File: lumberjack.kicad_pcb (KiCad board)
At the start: 2 copper layers, 285.4 x 94.9 mm, 156 parts, among them J1 USB, J2 AVR_ISP_6, J3 JST, SW1 RESET, SW2 BOOT, U1 ATMEGA328-PU, Y1 16MHz

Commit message: Update lumberjack.kicad_pcb
Updated PCB file, removed all traces
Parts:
- removed C1, C2: 22p, Capacitor_THT:C_Disc_D3.0mm_W1.6mm_P2.50mm
- removed C3: 4.7u, Capacitor_THT:CP_Radial_D4.0mm_P1.50mm
- removed C4, C5: 100n, Capacitor_THT:C_Disc_D4.3mm_W1.9mm_P5.00mm
- removed D1, D10, D11, D12, D13, D14, D15, D16, D17, D18, D19, D2, D20, D21, D22, D23, D24, D25, D26, D27, D28, D29, D3, D30, D31, D32, D33, D34, D35, D36, D37, D38, D39, D4, D40, D41, D42, D43, D44, D45, D46, D47, D48, D49, D5, D50, D51, D52, D53, D54, D55, D56, D57, D58, D59, D6, D60, D7, D8, D9: 1N4148, Diode_THT:D_DO-35_SOD27_P7.62mm_Horizontal
- removed D61, D62: 3.6V, Diode_THT:D_DO-35_SOD27_P7.62mm_Horizontal
- removed F1: 100mA, Fuse:Fuse_Bourns_MF-RHT100
- removed J2: AVR_ISP_6, Connector_PinHeader_2.54mm:PinHeader_2x03_P2.54mm_Vertical
- removed J3: JST, Connector_JST:JST_SH_SM04B-SRSS-TB_1x04-1MP_P1.00mm_Horizontal
- removed LED2: GREEN, LED_THT:LED_D3.0mm
- removed REF**: flags, lumberjack:Flags
- removed REF**: OSHW-Logo_7.5x8mm_Copper, Symbol:OSHW-Logo_7.5x8mm_Copper
- removed SW1: RESET, Button_Switch_THT:SW_PUSH_6mm
- removed SW2: BOOT, Button_Switch_THT:SW_PUSH_6mm
- removed Y1: 16MHz, Crystal:Crystal_HC49-4H_Vertical
- added JBtn1: Conn_01x06_Male, Connector_PinSocket_2.54mm:PinSocket_1x06_P2.54mm_Vertical, F.Cu at (135.9, 17.8)
- added JBtn2: Conn_01x06_Male, Connector_PinSocket_2.54mm:PinSocket_1x06_P2.54mm_Vertical, F.Cu at (108.3, 17.8)
- added JConn1: Conn_01x06_Male, Connector_PinSocket_2.54mm:PinSocket_1x06_P2.54mm_Vertical, F.Cu at (66.0, 38.1)
- added JL1: Conn_01x06_Male, Connector_PinSocket_2.54mm:PinSocket_1x06_P2.54mm_Vertical, F.Cu at (108.3, 35.1)
- added JL2: Conn_01x06_Male, Connector_PinSocket_2.54mm:PinSocket_1x06_P2.54mm_Vertical, F.Cu at (122.1, 17.8)
- added JL3: Conn_01x06_Male, Connector_PinSocket_2.54mm:PinSocket_1x06_P2.54mm_Vertical, F.Cu at (112.9, 35.1)
- added JL4: Conn_01x06_Male, Connector_PinSocket_2.54mm:PinSocket_1x06_P2.54mm_Vertical, F.Cu at (126.7, 17.8)
- added JL5: Conn_01x06_Male, Connector_PinSocket_2.54mm:PinSocket_1x06_P2.54mm_Vertical, F.Cu at (117.5, 35.1)
- added JR1: Conn_01x06_Male, Connector_PinSocket_2.54mm:PinSocket_1x06_P2.54mm_Vertical, F.Cu at (131.3, 17.8)
- added JR2: Conn_01x06_Male, Connector_PinSocket_2.54mm:PinSocket_1x06_P2.54mm_Vertical, F.Cu at (112.9, 17.8)
- added JR3: Conn_01x06_Male, Connector_PinSocket_2.54mm:PinSocket_1x06_P2.54mm_Vertical, F.Cu at (140.5, 17.8)
- added JR4: Conn_01x06_Male, Connector_PinSocket_2.54mm:PinSocket_1x06_P2.54mm_Vertical, F.Cu at (122.1, 35.1)
- added JR5: Conn_01x06_Male, Connector_PinSocket_2.54mm:PinSocket_1x06_P2.54mm_Vertical, F.Cu at (157.5, 31.8)
- added R10: 47k, Resistor_THT:R_Axial_DIN0204_L3.6mm_D1.6mm_P7.62mm_Horizontal, F.Cu at (173.3, 19.2)
- added R11: 47k, Resistor_THT:R_Axial_DIN0204_L3.6mm_D1.6mm_P7.62mm_Horizontal, F.Cu at (173.3, 22.4)
- added R12: 47k, Resistor_THT:R_Axial_DIN0204_L3.6mm_D1.6mm_P7.62mm_Horizontal, F.Cu at (173.3, 25.5)
- added R13: 1.5k, Resistor_THT:R_Axial_DIN0204_L3.6mm_D1.6mm_P7.62mm_Horizontal, F.Cu at (144.2, 17.0)
- added R9: 47k, Resistor_THT:R_Axial_DIN0204_L3.6mm_D1.6mm_P7.62mm_Horizontal, F.Cu at (173.3, 16.1)
- added U2: 4021, Package_DIP:DIP-16_W7.62mm_LongPads, F.Cu at (96.3, 17.5)
- J1: value USB -> RJ45; footprint lumberjack:USB_Hybrid_THT -> Connector_RJ:RJ45_Amphenol_54602-x08_Horizontal
- R1, R7, R8: value 1.5k -> 47k
- R2, R3: value 75R -> 47k
- R4: value 10k -> 47k
- R5, R6: value 5.1k -> 47k
- U1: value ATMEGA328-PU -> 4021; footprint Package_DIP:DIP-28_W7.62mm -> Package_DIP:DIP-16_W7.62mm_LongPads
- moved R6 128.1 mm to (169.5, 32.3), turned to 180 degrees
- moved R5 126.5 mm to (169.5, 29.9), turned to 180 degrees
- moved U1 88.1 mm to (83.7, 17.0)
- moved R4 87.9 mm to (168.8, 18.9)
- moved R1 87.9 mm to (161.1, 26.1)
- moved R2 87.9 mm to (161.1, 23.7)
- moved R3 87.9 mm to (161.1, 21.3)
- moved J1 43.7 mm to (57.1, 30.5)
- moved R7 41.5 mm to (181.8, 31.7)
- moved R8 34.9 mm to (181.5, 29.1)
- moved LED1 20.6 mm to (146.1, 43.2)
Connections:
- 2u_MX30 pad 1: Net-(2u_MX30-Pad1) -> GND
- 2u_MX30 pad 2: /COL4 -> /L5.6
- 2u_MX60 pad 1: Net-(2u_MX60-Pad1) -> GND
- 2u_MX60 pad 2: /COL9 -> /R5.1
- MX1 pad 1: Net-(D1-Pad2) -> GND
- MX1 pad 2: /COL0 -> /L1.1
- MX10 pad 1: Net-(D10-Pad2) -> GND
- MX10 pad 2: /COL1 -> /L4.2
- MX11 pad 1: Net-(D11-Pad2) -> GND
- MX11 pad 2: /COL1 -> /L4.3
- MX12 pad 1: Net-(D12-Pad2) -> GND
- MX12 pad 2: /COL1 -> /L5.3
- MX13 pad 1: Net-(D13-Pad2) -> GND
- MX13 pad 2: /COL2 -> /L1.3
- MX14 pad 1: Net-(D14-Pad2) -> GND
- MX14 pad 2: /COL2 -> /L2.3
- MX15 pad 1: Net-(D15-Pad2) -> GND
- MX15 pad 2: /COL2 -> /L3.3
- MX16 pad 1: Net-(D16-Pad2) -> GND
- MX16 pad 2: /COL2 -> /L3.4
- MX17 pad 1: Net-(D17-Pad2) -> GND
- MX17 pad 2: /COL2 -> /L4.4
- MX18 pad 1: Net-(D18-Pad2) -> GND
- MX18 pad 2: /COL2 -> /L5.4
- MX19 pad 1: Net-(D19-Pad2) -> GND
- MX19 pad 2: /COL3 -> /L1.4
- MX2 pad 1: Net-(D2-Pad2) -> GND
- MX2 pad 2: /COL0 -> /L2.1
- MX20 pad 1: Net-(D20-Pad2) -> GND
- MX20 pad 2: /COL3 -> /L2.4
- MX21 pad 1: Net-(D21-Pad2) -> GND
- MX21 pad 2: /COL3 -> /L2.5
- MX22 pad 1: Net-(D22-Pad2) -> GND
- MX22 pad 2: /COL3 -> /L3.5
- MX23 pad 1: Net-(D23-Pad2) -> GND
- MX23 pad 2: /COL3 -> /L4.5
- MX24 pad 1: Net-(D24-Pad2) -> GND
- MX24 pad 2: /COL3 -> /L5.5
- MX25 pad 1: Net-(D25-Pad2) -> GND
- MX25 pad 2: /COL4 -> /L1.5
- MX26 pad 1: Net-(D26-Pad2) -> GND
- MX26 pad 2: /COL4 -> /L1.6
- MX27 pad 1: Net-(D27-Pad2) -> GND
- MX27 pad 2: /COL4 -> /L2.6
- MX28 pad 1: Net-(D28-Pad2) -> GND
- MX28 pad 2: /COL4 -> /L3.6
- MX29 pad 1: Net-(D29-Pad2) -> GND
- MX29 pad 2: /COL4 -> /L4.6
- MX3 pad 1: Net-(D3-Pad2) -> GND
- MX3 pad 2: /COL0 -> /L3.1
- MX30 pad 1: Net-(2u_MX30-Pad1) -> GND
- MX30 pad 2: /COL4 -> /L5.6
- MX31 pad 1: Net-(D31-Pad2) -> GND
- MX31 pad 2: /COL5 -> /R1.6
- MX32 pad 1: Net-(D32-Pad2) -> GND
- MX32 pad 2: /COL5 -> /R2.6
- MX33 pad 1: Net-(D33-Pad2) -> GND
- MX33 pad 2: /COL5 -> /R3.6
- MX34 pad 1: Net-(D34-Pad2) -> GND
- MX34 pad 2: /COL5 -> /R4.6
- MX35 pad 1: Net-(D35-Pad2) -> GND
- MX35 pad 2: /COL5 -> /R5.6
- MX36 pad 1: Net-(D36-Pad2) -> GND
- MX36 pad 2: /COL5 -> /R5.5
- MX37 pad 1: Net-(D37-Pad2) -> GND
- MX37 pad 2: /COL6 -> /R1.5
- MX38 pad 1: Net-(D38-Pad2) -> GND
- MX38 pad 2: /COL6 -> /R2.5
- MX39 pad 1: Net-(D39-Pad2) -> GND
- MX39 pad 2: /COL6 -> /R3.5
- MX4 pad 1: Net-(D4-Pad2) -> GND
- MX4 pad 2: /COL0 -> /L4.1
- MX40 pad 1: Net-(D40-Pad2) -> GND
- MX40 pad 2: /COL6 -> /R4.5
- MX41 pad 1: Net-(D41-Pad2) -> GND
- MX41 pad 2: /COL6 -> /R4.4
- MX42 pad 1: Net-(D42-Pad2) -> GND
- MX42 pad 2: /COL6 -> /R5.4
- MX43 pad 1: Net-(D43-Pad2) -> GND
- MX43 pad 2: /COL7 -> /R1.4
- MX44 pad 1: Net-(D44-Pad2) -> GND
- MX44 pad 2: /COL7 -> /R2.4
- MX45 pad 1: Net-(D45-Pad2) -> GND
- MX45 pad 2: /COL7 -> /R3.4
- MX46 pad 1: Net-(D46-Pad2) -> GND
- MX46 pad 2: /COL7 -> /R3.3
- MX47 pad 1: Net-(D47-Pad2) -> GND
- MX47 pad 2: /COL7 -> /R4.3
- MX48 pad 1: Net-(D48-Pad2) -> GND
- MX48 pad 2: /COL7 -> /R5.3
- MX49 pad 1: Net-(D49-Pad2) -> GND
- MX49 pad 2: /COL8 -> /R1.3
- MX5 pad 1: Net-(D5-Pad2) -> GND
- MX5 pad 2: /COL0 -> /L5.1
- MX50 pad 1: Net-(D50-Pad2) -> GND
- MX50 pad 2: /COL8 -> /R2.3
- MX51 pad 1: Net-(D51-Pad2) -> GND
- MX51 pad 2: /COL8 -> /R2.2
- MX52 pad 1: Net-(D52-Pad2) -> GND
- MX52 pad 2: /COL8 -> /R3.2
- MX53 pad 1: Net-(D53-Pad2) -> GND
- MX53 pad 2: /COL8 -> /R4.2
- MX54 pad 1: Net-(D54-Pad2) -> GND
- MX54 pad 2: /COL8 -> /R5.2
- MX55 pad 1: Net-(D55-Pad2) -> GND
- MX55 pad 2: /COL9 -> /R1.2
- MX56 pad 1: Net-(D56-Pad2) -> GND
- MX56 pad 2: /COL9 -> /R1.1
- MX57 pad 1: Net-(D57-Pad2) -> GND
- MX57 pad 2: /COL9 -> /R2.1
- MX58 pad 1: Net-(D58-Pad2) -> GND
- MX58 pad 2: /COL9 -> /R3.1
- MX59 pad 1: Net-(D59-Pad2) -> GND
- MX59 pad 2: /COL9 -> /R4.1
- MX6 pad 1: Net-(D6-Pad2) -> GND
- MX6 pad 2: /COL0 -> /L5.2
- MX60 pad 1: Net-(2u_MX60-Pad1) -> GND
- MX60 pad 2: /COL9 -> /R5.1
- MX7 pad 1: Net-(D7-Pad2) -> GND
- MX7 pad 2: /COL1 -> /L1.2
- MX8 pad 1: Net-(D8-Pad2) -> GND
- MX8 pad 2: /COL1 -> /L2.2
- MX9 pad 1: Net-(D9-Pad2) -> GND
- MX9 pad 2: /COL1 -> /L3.2
- R1 pad 1: Net-(D67-Pad1) -> /BtnUp
- R2 pad 1: Net-(D66-Pad1) -> /BtnDown
- R2 pad 2: /USB_D+ -> +5V
- R3 pad 1: Net-(D67-Pad1) -> /BtnLeft
- R3 pad 2: /USB_D- -> +5V
- R4 pad 1: +5V -> /BtnRight
- R4 pad 2: /RESET -> +5V
- R5 pad 1: GND -> /BtnStart
- R5 pad 2: Net-(J1-PadCC1) -> +5V
- R6 pad 1: GND -> /BtnSelect
- R6 pad 2: Net-(J1-PadCC2) -> +5V
- R7 pad 1: /LED1 -> /BtnA
- R7 pad 2: Net-(LED1-Pad2) -> +5V
- R8 pad 1: /LED2 -> /BtnB
- R8 pad 2: Net-(LED2-Pad2) -> +5V
- U1 pad 1: /RESET -> /BtnB
- U1 pad 10: Net-(C1-Pad1) -> /clock
- U1 pad 11: /COL3 -> Net-(U1-Pad11)
- U1 pad 12: /COL2 -> Net-(U1-Pad12)
- U1 pad 13: /COL1 -> /BtnStart
- U1 pad 14: /COL0 -> /BtnSelect
- U1 pad 15: /ROW5 -> /BtnY
- U1 pad 16: /ROW4 -> +5V
- U1 pad 2: /COL6 -> Net-(U1-Pad2)
- U1 pad 3: /COL5 -> /data
- U1 pad 4: /USB_D+ -> /BtnUp
- U1 pad 5: /USB_D- -> /BtnDown
- U1 pad 6: /COL4 -> /BtnLeft
- U1 pad 7: +5V -> /BtnRight
- U1 pad 9: Net-(C2-Pad1) -> /reset
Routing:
- net /COL0: track 259.9 -> 0.00 mm
- net /COL5: track 237.0 -> 0.00 mm
- net /COL1: track 230.1 -> 0.00 mm
- net /COL6: track 211.7 -> 0.00 mm
- net Net-(D67-Pad1): track 191.9 -> 0.00 mm, vias 1 -> 0
- net Net-(D66-Pad1): track 191.8 -> 0.00 mm, vias 2 -> 0
- net /COL3: track 187.7 -> 0.00 mm
- net /COL2: track 185.5 -> 0.00 mm
- net /COL7: track 182.0 -> 0.00 mm
- net Net-(F1-Pad1): track 176.4 -> 0.00 mm
- net /ROW3: track 166.2 -> 0.00 mm
- net /COL4: track 159.8 -> 0.00 mm
- net /COL8: track 144.3 -> 0.00 mm
- net /COL9: track 132.7 -> 0.00 mm
- net Net-(D35-Pad2): track 129.2 -> 0.00 mm
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- removed copper zone on B.Cu, net GND
- removed copper zone on F.Cu, net GND
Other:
- board text removed: "GND"
- board text removed: "ISP"
- board text removed: "MISO"
- board text removed: "MOSI"
- board text removed: "RST"
- board text removed: "SCLK"
- board text removed: "VCC"

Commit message: Update lumberjack.kicad_pcb
PCB before infill
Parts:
- removed H1, H2, H3, H4: M2, lumberjack:MountingHole_M2
- added C1: 0.1uF, Capacitor_THT:C_Disc_D5.0mm_W2.5mm_P2.50mm, F.Cu at (134.6, 137.2)
- added C10: 0.1uF, Capacitor_THT:C_Disc_D5.0mm_W2.5mm_P2.50mm, F.Cu at (158.8, 116.8)
- added C11: 0.1uF, Capacitor_THT:C_Disc_D5.0mm_W2.5mm_P2.50mm, F.Cu at (166.4, 116.9)
- added C12: 0.1uF, Capacitor_THT:C_Disc_D5.0mm_W2.5mm_P2.50mm, F.Cu at (174.0, 116.8)
- added C13: 0.1uF, Capacitor_THT:C_Disc_D5.0mm_W2.5mm_P2.50mm, F.Cu at (171.7, 79.2)
- added C14: 0.1uF, Capacitor_THT:C_Disc_D5.0mm_W2.5mm_P2.50mm, F.Cu at (156.5, 79.2)
- added C15: 0.1uF, Capacitor_THT:C_Disc_D5.0mm_W2.5mm_P2.50mm, F.Cu at (143.3, 79.2)
- added C16: 0.1uF, Capacitor_THT:C_Disc_D5.0mm_W2.5mm_P2.50mm, F.Cu at (132.1, 79.2)
- added C17: 0.1uF, Capacitor_THT:C_Disc_D5.0mm_W2.5mm_P2.50mm, F.Cu at (127.0, 60.9)
- added C18: 0.1uF, Capacitor_THT:C_Disc_D5.0mm_W2.5mm_P2.50mm, F.Cu at (175.8, 57.4)
- added C2: 0.1uF, Capacitor_THT:C_Disc_D5.0mm_W2.5mm_P2.50mm, F.Cu at (142.2, 137.2)
- added C3: 0.1uF, Capacitor_THT:C_Disc_D5.0mm_W2.5mm_P2.50mm, F.Cu at (149.9, 137.2)
- added C4: 0.1uF, Capacitor_THT:C_Disc_D5.0mm_W2.5mm_P2.50mm, F.Cu at (134.6, 116.9)
- added C5: 0.1uF, Capacitor_THT:C_Disc_D5.0mm_W2.5mm_P2.50mm, F.Cu at (142.2, 116.8)
- added C6: 0.1uF, Capacitor_THT:C_Disc_D5.0mm_W2.5mm_P2.50mm, F.Cu at (149.9, 116.8)
- added C7: 0.1uF, Capacitor_THT:C_Disc_D5.0mm_W2.5mm_P2.50mm, F.Cu at (158.8, 137.2)
- added C8: 0.1uF, Capacitor_THT:C_Disc_D5.0mm_W2.5mm_P2.50mm, F.Cu at (166.4, 137.2)
- added C9: 0.1uF, Capacitor_THT:C_Disc_D5.0mm_W2.5mm_P2.50mm, F.Cu at (174.0, 137.2)
- added D1: 1N4148, Diode_THT:D_DO-35_SOD27_P7.62mm_Horizontal, F.Cu at (130.8, 137.2)
- added D10: 1N4148, Diode_THT:D_DO-35_SOD27_P7.62mm_Horizontal, F.Cu at (154.9, 116.8)
- added D11: 1N4148, Diode_THT:D_DO-35_SOD27_P7.62mm_Horizontal, F.Cu at (162.6, 116.8)
- added D12: 1N4148, Diode_THT:D_DO-35_SOD27_P7.62mm_Horizontal, F.Cu at (170.2, 116.8)
- added D2: 1N4148, Diode_THT:D_DO-35_SOD27_P7.62mm_Horizontal, F.Cu at (138.4, 137.2)
- added D3: 1N4148, Diode_THT:D_DO-35_SOD27_P7.62mm_Horizontal, F.Cu at (146.1, 137.2)
- added D4: 1N4148, Diode_THT:D_DO-35_SOD27_P7.62mm_Horizontal, F.Cu at (130.8, 116.8)
- added D5: 1N4148, Diode_THT:D_DO-35_SOD27_P7.62mm_Horizontal, F.Cu at (138.4, 116.8)
- added D6: 1N4148, Diode_THT:D_DO-35_SOD27_P7.62mm_Horizontal, F.Cu at (146.1, 116.8)
- added D7: 1N4148, Diode_THT:D_DO-35_SOD27_P7.62mm_Horizontal, F.Cu at (154.9, 137.2)
- added D8: 1N4148, Diode_THT:D_DO-35_SOD27_P7.62mm_Horizontal, F.Cu at (162.6, 137.2)
- added D9: 1N4148, Diode_THT:D_DO-35_SOD27_P7.62mm_Horizontal, F.Cu at (170.2, 137.2)
- added R100: 1.5k, Resistor_THT:R_Axial_DIN0207_L6.3mm_D2.5mm_P7.62mm_Horizontal, F.Cu at (148.8, 102.6)
- added R14: 205k, Resistor_THT:R_Axial_DIN0207_L6.3mm_D2.5mm_P7.62mm_Horizontal, F.Cu at (158.8, 127.0)
- added R15: 46.4k, Resistor_THT:R_Axial_DIN0207_L6.3mm_D2.5mm_P7.62mm_Horizontal, F.Cu at (162.6, 134.6)
- added R16: 205k, Resistor_THT:R_Axial_DIN0207_L6.3mm_D2.5mm_P7.62mm_Horizontal, F.Cu at (166.4, 127.0)
- added R17: 46.4k, Resistor_THT:R_Axial_DIN0207_L6.3mm_D2.5mm_P7.62mm_Horizontal, F.Cu at (170.2, 134.6)
- added R18: 205k, Resistor_THT:R_Axial_DIN0207_L6.3mm_D2.5mm_P7.62mm_Horizontal, F.Cu at (174.0, 127.0)
- added R19: 46.4k, Resistor_THT:R_Axial_DIN0207_L6.3mm_D2.5mm_P7.62mm_Horizontal, F.Cu at (154.9, 114.3)
- added R20: 205k, Resistor_THT:R_Axial_DIN0207_L6.3mm_D2.5mm_P7.62mm_Horizontal, F.Cu at (158.8, 106.7)
- added R21: 46.4k, Resistor_THT:R_Axial_DIN0207_L6.3mm_D2.5mm_P7.62mm_Horizontal, F.Cu at (162.6, 114.3)
- added R22: 205k, Resistor_THT:R_Axial_DIN0207_L6.3mm_D2.5mm_P7.62mm_Horizontal, F.Cu at (166.4, 106.7)
- added R23: 46.4k, Resistor_THT:R_Axial_DIN0207_L6.3mm_D2.5mm_P7.62mm_Horizontal, F.Cu at (170.2, 114.3)
- added R24: 205k, Resistor_THT:R_Axial_DIN0207_L6.3mm_D2.5mm_P7.62mm_Horizontal, F.Cu at (174.0, 106.7)
- added U3: 74HC14, Package_DIP:DIP-14_W7.62mm_LongPads, F.Cu at (154.9, 82.5)
- added U4: 74HC14, Package_DIP:DIP-14_W7.62mm_LongPads, F.Cu at (166.4, 82.5)
- added U5: 4021, Package_DIP:DIP-16_W7.62mm_LongPads, F.Cu at (132.1, 57.1)
- added U6: 4021, Package_DIP:DIP-16_W7.62mm_LongPads, F.Cu at (163.8, 57.1)
- R1, R11, R3, R5, R7, R9: value 47k -> 46.4k; footprint Resistor_THT:R_Axial_DIN0204_L3.6mm_D1.6mm_P7.62mm_Horizontal -> Resistor_THT:R_Axial_DIN0207_L6.3mm_D2.5mm_P7.62mm_Horizontal
- R10, R12, R2, R4, R6, R8: value 47k -> 205k; footprint Resistor_THT:R_Axial_DIN0204_L3.6mm_D1.6mm_P7.62mm_Horizontal -> Resistor_THT:R_Axial_DIN0207_L6.3mm_D2.5mm_P7.62mm_Horizontal
- R13: value 1.5k -> 46.4k; footprint Resistor_THT:R_Axial_DIN0204_L3.6mm_D1.6mm_P7.62mm_Horizontal -> Resistor_THT:R_Axial_DIN0207_L6.3mm_D2.5mm_P7.62mm_Horizontal
- U1, U2: value 4021 -> 74HC14; footprint Package_DIP:DIP-16_W7.62mm_LongPads -> Package_DIP:DIP-14_W7.62mm_LongPads
- moved JBtn2 140.1 mm to (161.5, 147.3), turned to 90 degrees
- moved JBtn1 129.5 mm to (137.2, 147.3), turned to 90 degrees
- moved R13 118.1 mm to (154.9, 134.6), turned to 90 degrees
- moved R3 115.6 mm to (138.4, 134.6), turned to 90 degrees
- moved R1 112.7 mm to (130.8, 134.6), turned to 90 degrees
- moved R4 111.3 mm to (142.2, 127.0), turned to 270 degrees
- moved R5 107.3 mm to (146.1, 134.6), turned to 90 degrees
- moved R2 106.7 mm to (134.6, 127.0), turned to 270 degrees
- moved JR5 104.9 mm to (177.8, 134.6)
- moved R9 104.2 mm to (138.4, 114.3), turned to 90 degrees
- moved JL4 100.3 mm to (127.0, 118.1)
- moved JL5 100.0 mm to (127.0, 134.6)
- moved JR4 100.0 mm to (177.8, 118.1)
- moved JConn1 99.8 mm to (158.5, 75.7)
- moved J1 98.4 mm to (147.3, 69.8)
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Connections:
- R1 pad 2: +5V -> Net-(C1-Pad1)
- R10 pad 1: /BtnY -> +5V
- R10 pad 2: +5V -> /BtnStart
- R11 pad 1: /BtnL -> /BtnSelect
- R11 pad 2: +5V -> Net-(C6-Pad1)
- R12 pad 1: /RtnR -> +5V
- R12 pad 2: +5V -> /BtnSelect
- R13 pad 1: +5V -> /BtnA
- R13 pad 2: Net-(LED1-Pad2) -> Net-(C7-Pad1)
- R2 pad 1: /BtnDown -> +5V
- R2 pad 2: +5V -> /BtnUp
- R3 pad 1: /BtnLeft -> /BtnDown
- R3 pad 2: +5V -> Net-(C2-Pad1)
- R4 pad 1: /BtnRight -> +5V
- R4 pad 2: +5V -> /BtnDown
- R5 pad 1: /BtnStart -> /BtnLeft
- R5 pad 2: +5V -> Net-(C3-Pad1)
- R6 pad 1: /BtnSelect -> +5V
- R6 pad 2: +5V -> /BtnLeft
- R7 pad 1: /BtnA -> /BtnRight
- R7 pad 2: +5V -> Net-(C4-Pad1)
- R8 pad 1: /BtnB -> +5V
- R8 pad 2: +5V -> /BtnRight
- R9 pad 1: /BtnX -> /BtnStart
- R9 pad 2: +5V -> Net-(C5-Pad1)
- U1 pad 1: /BtnB -> Net-(C1-Pad1)
- U1 pad 10: /clock -> Net-(U1-Pad10)
- U1 pad 11: Net-(U1-Pad11) -> Net-(C3-Pad1)
- U1 pad 12: Net-(U1-Pad12) -> /BtnLeftDebounced
- U1 pad 13: /BtnStart -> Net-(U1-Pad10)
- U1 pad 14: /BtnSelect -> +5V
- U1 pad 3: /data -> Net-(U1-Pad2)
- U1 pad 4: /BtnUp -> /BtnUpDebounced
- U1 pad 5: /BtnDown -> Net-(C2-Pad1)
- U1 pad 6: /BtnLeft -> Net-(U1-Pad6)
- U1 pad 7: /BtnRight -> GND
- U1 pad 8: GND -> /BtnDownDebounced
- U1 pad 9: /reset -> Net-(U1-Pad6)
- U2 pad 1: /BtnA -> Net-(C4-Pad1)
- U2 pad 10: /clock -> Net-(U2-Pad10)
- U2 pad 11: Net-(U2-Pad11) -> Net-(C6-Pad1)
- U2 pad 12: Net-(U2-Pad12) -> /BtnSelectDebounced
- U2 pad 13: /BtnR -> Net-(U2-Pad10)
- U2 pad 14: /BtnL -> +5V
- U2 pad 3: Net-(U1-Pad11) -> Net-(U2-Pad2)
- U2 pad 4: Net-(U2-Pad4) -> /BtnRightDebounced
- U2 pad 5: Net-(U2-Pad5) -> Net-(C5-Pad1)
- U2 pad 7: Net-(U2-Pad7) -> GND
- U2 pad 8: GND -> /BtnStartDebounced
- U2 pad 9: /reset -> Net-(U2-Pad6)
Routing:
- net GND: track 0.00 -> 2345.3 mm, vias 1 -> 4
- net +5V: track 0.00 -> 278.6 mm
- net /L1.1: track 0.00 -> 124.2 mm
- net /L3.1: track 0.00 -> 121.7 mm
- net /L4.1: track 0.00 -> 121.6 mm
- net /L2.1: track 0.00 -> 120.7 mm
- net /R1.6: track 0.00 -> 118.0 mm
- net /L5.1: track 0.00 -> 117.8 mm
- net /R2.6: track 0.00 -> 116.6 mm
- net /R3.6: track 0.00 -> 115.5 mm
- net /R4.6: track 0.00 -> 109.1 mm
- net /R5.6: track 0.00 -> 108.0 mm
- net /L1.2: track 0.00 -> 107.0 mm
- net /L3.2: track 0.00 -> 104.4 mm
- net /L4.2: track 0.00 -> 103.0 mm
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
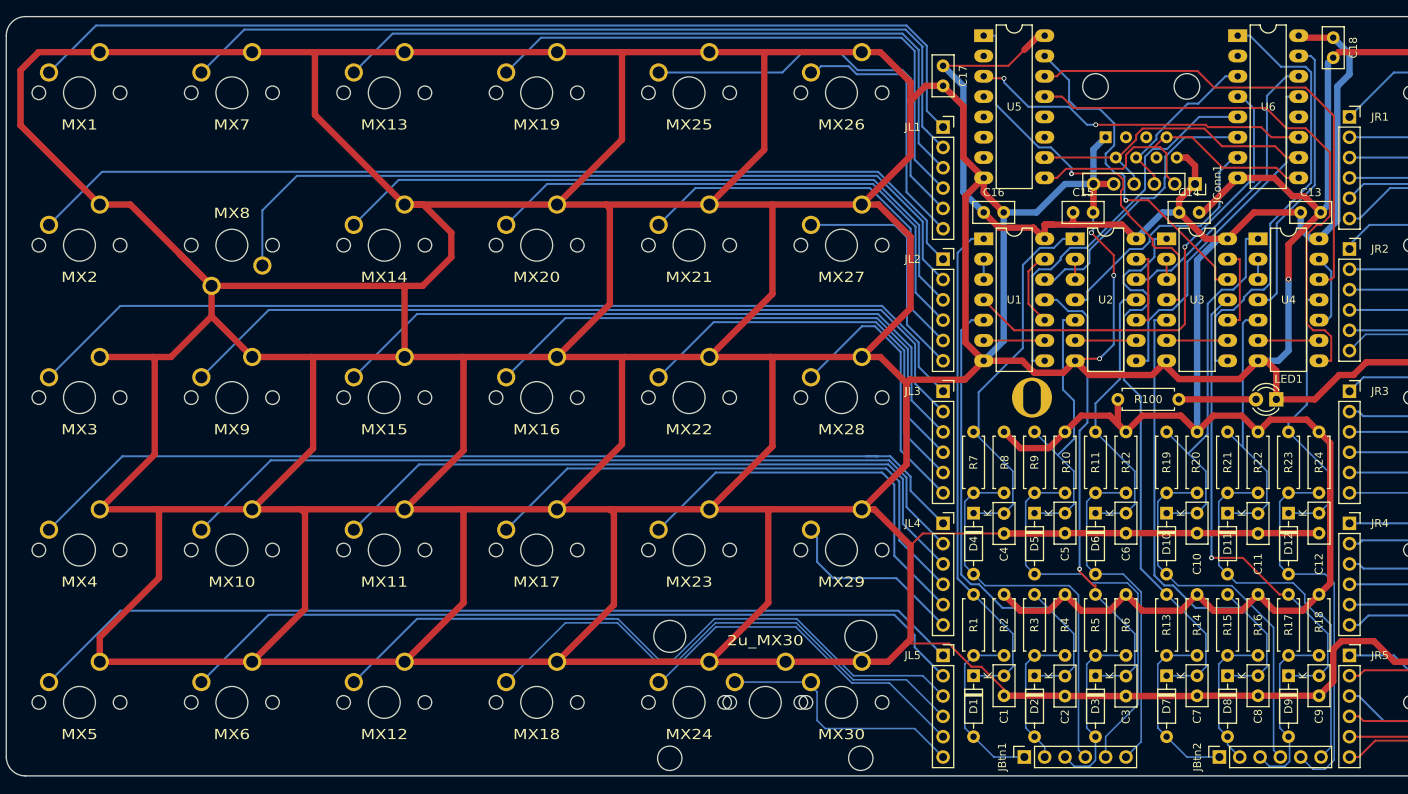
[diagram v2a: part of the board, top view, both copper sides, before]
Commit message: Couple 'o rule fixes
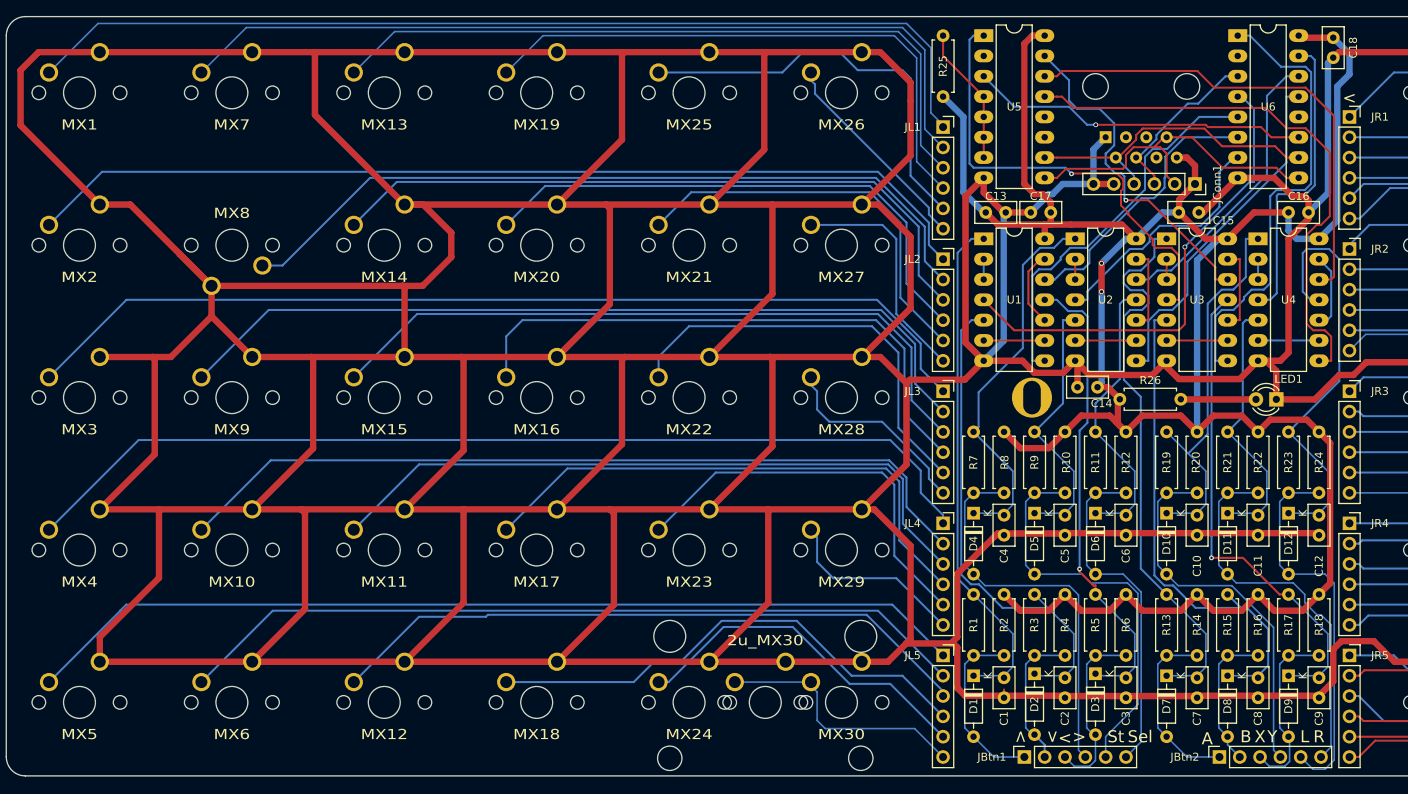
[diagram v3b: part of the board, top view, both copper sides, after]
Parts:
- removed R100: 1.5k, Resistor_THT:R_Axial_DIN0207_L6.3mm_D2.5mm_P7.62mm_Horizontal
- added R25: 205k, Resistor_THT:R_Axial_DIN0207_L6.3mm_D2.5mm_P7.62mm_Horizontal, F.Cu at (127.0, 64.8)
- added R26: 470, Resistor_THT:R_Axial_DIN0207_L6.3mm_D2.5mm_P7.62mm_Horizontal, F.Cu at (149.1, 102.6)
- moved C13 39.4 mm to (132.3, 79.2)
- moved C16 38.1 mm to (170.2, 79.2)
- moved C14 24.1 mm to (146.3, 101.1), turned to 180 degrees
- moved C17 22.7 mm to (140.5, 79.2), turned to 180 degrees
- moved C15 13.2 mm to (156.5, 79.2)
- moved C1 0.25 mm to (134.6, 137.4)
- moved C10 0.25 mm to (158.8, 117.1)
- moved C12 0.25 mm to (174.0, 117.1)
- moved C5 0.25 mm to (142.2, 117.1)
- moved C6 0.25 mm to (149.9, 117.1)
- moved C7 0.25 mm to (158.8, 137.4)
- moved C8 0.25 mm to (166.4, 137.4)
- moved C9 0.25 mm to (174.0, 137.4)
- moved D2 0.25 mm to (138.4, 136.9)
- moved D3 0.25 mm to (146.1, 136.9)
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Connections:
- U5 pad 4: Net-(U5-Pad4) -> Net-(R25-Pad2)
- U5 pad 5: Net-(U5-Pad5) -> Net-(R25-Pad2)
- U5 pad 6: Net-(U5-Pad6) -> Net-(R25-Pad2)
- U5 pad 7: Net-(U5-Pad7) -> Net-(R25-Pad2)
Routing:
- net GND: track 2345.3 -> 2311.0 mm, vias 4 -> 0
- net +5V: track 278.6 -> 311.0 mm, vias 0 -> 2
- net Net-(C12-Pad1): track 35.4 -> 53.3 mm
- net Net-(R25-Pad2): track 0.00 -> 17.3 mm
- net /L3.6: track 35.0 -> 25.2 mm
- net /BtnADebounced: track 50.9 -> 58.4 mm
- net /L1.6: track 33.5 -> 26.4 mm
- net /L2.2: track 101.9 -> 97.4 mm
- net /L5.4: track 66.6 -> 62.7 mm
- net /L5.3: track 85.1 -> 81.7 mm
- net Net-(C5-Pad1): track 36.3 -> 33.4 mm
- net /L3.4: track 69.6 -> 72.2 mm
- net /BtnBDebounced: track 55.4 -> 57.5 mm
- net /BtnYDebounced: track 36.0 -> 38.1 mm
- net /L4.1: track 121.6 -> 122.9 mm
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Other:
- board text added: ">"
- board text added: "A"
- board text added: "B"
- board text added: "L"
- board text added: "R"
- board text added: "Sel"
- board text added: "St"
- board text added: "X"
- board text added: "Y"

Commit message: Ready for a ground plane? 2
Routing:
- net /BtnXDebounced: track 43.5 -> 42.2 mm
- net Net-(U3-Pad10): track 10.7 -> 9.39 mm
- net Net-(U2-Pad10): track 10.7 -> 9.54 mm
